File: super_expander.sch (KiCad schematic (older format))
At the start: 48 parts, among them SW1 MCU_RESET, U33 ATtiny85-20SU, U34 PCA9548APW, Y1 8MHz

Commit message: Continue Routing
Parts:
- added C35, C36, C37, C38: 100nF, Capacitor_SMD:C_0603_1608Metric, symbol Device:C_Small
- added C41, C42: 100uF, Capacitor_THT:CP_Radial_D6.3mm_P2.50mm, symbol Device:CP
- added D1: 1N5819, Diode_SMD:D_SOD-123F, symbol Diode:1N5819
- added D2, D3: 0603ESDA-05N, Diode_SMD:D_0603_1608Metric, symbol Device:D_TVS
- added D4: LED_I2C, LED_SMD:LED_0603_1608Metric, symbol Device:LED
- added D5: ZMM6V2, Diode_SMD:D_MiniMELF, symbol Device:D_Zener
- added FB1, FB2: FCM1608KF-121T05, Inductor_SMD:L_0603_1608Metric, symbol Device:Ferrite_Bead_Small
- added J65: USB_B_Micro, Connector_USB:USB_Micro-B_Molex_47346-0001, symbol Connector:USB_B_Micro
- added J66, J67: I2C Passthrough, Connector_PinHeader_2.54mm:PinHeader_1x05_P2.54mm_Vertical, symbol Connector:Conn_01x05_Female
- added J68: Barrel_Jack_Switch, Connector_BarrelJack:BarrelJack_Horizontal, symbol Connector:Barrel_Jack_Switch
- added JP4, JP5, JP6, JP7: I2C BUF PASS, Resistor_SMD:R_0402_1005Metric, symbol Device:Jumper_NO_Small
- added Q1: IRF7410, Package_SO:SOIC-8_3.9x4.9mm_P1.27mm, symbol super_expander:IRF7410
- added R1: 1k, Resistor_SMD:R_0603_1608Metric, symbol Device:R
- added R2: 100k, Resistor_SMD:R_0603_1608Metric, symbol Device:R
- added U35: MCP2221A-I/ST, Package_SO:TSSOP-14_4.4x5mm_P0.65mm, symbol Interface_USB:MCP2221AxST
- added U36, U37: TCA9517, Package_SO:VSSOP-8_3.0x3.0mm_P0.65mm, symbol super_expander:TCA9517
- SW1: footprint Button_Switch_THT:SW_PUSH_6mm -> super_expander:TS-1101
- renumbered C35 to C39, C36 to C40
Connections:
- net +5V: now also C35.1, C36.1, C37.1, C38.1, C41.1, C42.1, D1.1 (K), D5.1 (K), J66.1 (Pin_1), J67.1 (Pin_1), Q1.1 (S), Q1.2 (S), Q1.3 (S), R1.1, U35.1 (VDD), U36.1 (VCCA), U36.5 (EN), U36.8 (VCCB), U37.1 (VCCA), U37.5 (EN), U37.8 (VCCB); no longer C16.1, C19.1, C20.1
- net GND: now also C35.2, C36.2, C37.2, C38.2, C41.2, C42.2, D2.2 (A2), D3.2 (A2), FB2.2, J65.5 (GND), J66.5 (Pin_5), J67.5 (Pin_5), J68.2, J68.3, R2.2, U35.14 (VSS), U36.4 (GND), U37.4 (GND)
- net ~RST: now also J66.4 (Pin_4), J67.4 (Pin_4), U35.7 (GP2)
- net SCL: now reaches U33.7 (PB2), U34.22 (SCL)
- net SCL: now also RN1.3 (R3.1), JP4.2, JP5.1, U35.10 (SCL), U36.7 (SCLB), U37.2 (SCLA); no longer RN1.4 (R4.1)
- net SDA: now reaches U33.5 (AREF/PB0), U34.23 (SDA)
- net SDA: now also RN1.1 (R1.1), JP6.2, JP7.1, U35.9 (SDA), U36.6 (SDAB), U37.3 (SDAA); no longer RN1.3 (R3.1)
- net ~MRST: now reaches SW1.1, U33.1 (~RESET~/PB5)
- net ~MRST: now also RN1.4 (R4.1), U35.4 (~RST); no longer RN1.1 (R1.1)
- new net: C16.1, C19.1, C20.1, U35.11 (VUSB)
- new net: D2.1 (A1), J65.2 (D-), U35.12 (D-)
- new net: D3.1 (A1), J65.3 (D+), U35.13 (D+)
- new net: D4.1 (K), U35.8 (GP3)
- new net: FB1.1, J65.1 (VBUS)
- new net: FB2.1, J65.6 (Shield)
- new net: D1.2 (A), FB1.2
- new net: D4.2 (A), R1.2
- new net: J66.2 (Pin_2), JP4.1, U36.2 (SCLA)
- new net: J66.3 (Pin_3), JP6.1, U36.3 (SDAA)
- new net: J67.3 (Pin_3), JP7.2, U37.6 (SDAB)
- new net: J67.2 (Pin_2), JP5.2, U37.7 (SCLB)
- new net: J68.1, Q1.5 (D), Q1.6 (D), Q1.7 (D), Q1.8 (D)
- new net: D5.2 (A), Q1.4 (G), R2.1
- no-connect marks 0 -> 5
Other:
- moved on the sheet: C15, C16, C17, C18, C19, C20, C21, C22, C23, C24, C25, C26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

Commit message: version 1
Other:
- note added: "Decoupling Caps"
- note added: "I2C Buffer"
- note added: "MCP2221 USB Control"
- note added: "MCU and I2C Mux"
- note added: "Power"
- moved on the sheet: C15, C16, C19, C20, C41, C42, D1, D2, D3, D4, D5, FB1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

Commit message: Add programming header
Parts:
- added J69: ICSP, Connector_PinHeader_2.54mm:PinHeader_2x03_P2.54mm_Vertical, symbol Connector_Generic:Conn_02x03_Odd_Even
- added RN134: 4k7, Resistor_SMD:R_Array_Convex_4x0603, symbol Device:R_Pack04
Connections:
- net +5V: now also J69.2 (Pin_2)
- net GND: now also J69.6 (Pin_6)
- net SCL: now also RN1.4 (R4.1), RN134.7 (R2.2); no longer RN1.3 (R3.1), U33.7 (PB2)
- net SDA: now also RN1.3 (R3.1), RN134.6 (R3.2); no longer RN1.1 (R1.1), U33.5 (AREF/PB0)
- net ~MRST: now also RN1.1 (R1.1), J69.5 (Pin_5); no longer RN1.4 (R4.1)
- net ~RST: now also RN134.8 (R1.2); no longer U33.6 (PB1)
- new net: J69.4 (Pin_4), RN134.3 (R3.1), U33.5 (AREF/PB0)
- new net: J69.1 (Pin_1), RN134.1 (R1.1), U33.6 (PB1)
- new net: J69.3 (Pin_3), RN134.2 (R2.1), U33.7 (PB2)
- no-connect marks 5 -> 7
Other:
- note added: "ATtiny85 MCU"
- note added: "I2C Mux"
- note removed: "MCU and I2C Mux"
- moved on the sheet: C39, C40, JP1, JP2, JP3, RN1, RN2, RN3, RN4, RN5, SW1, U33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

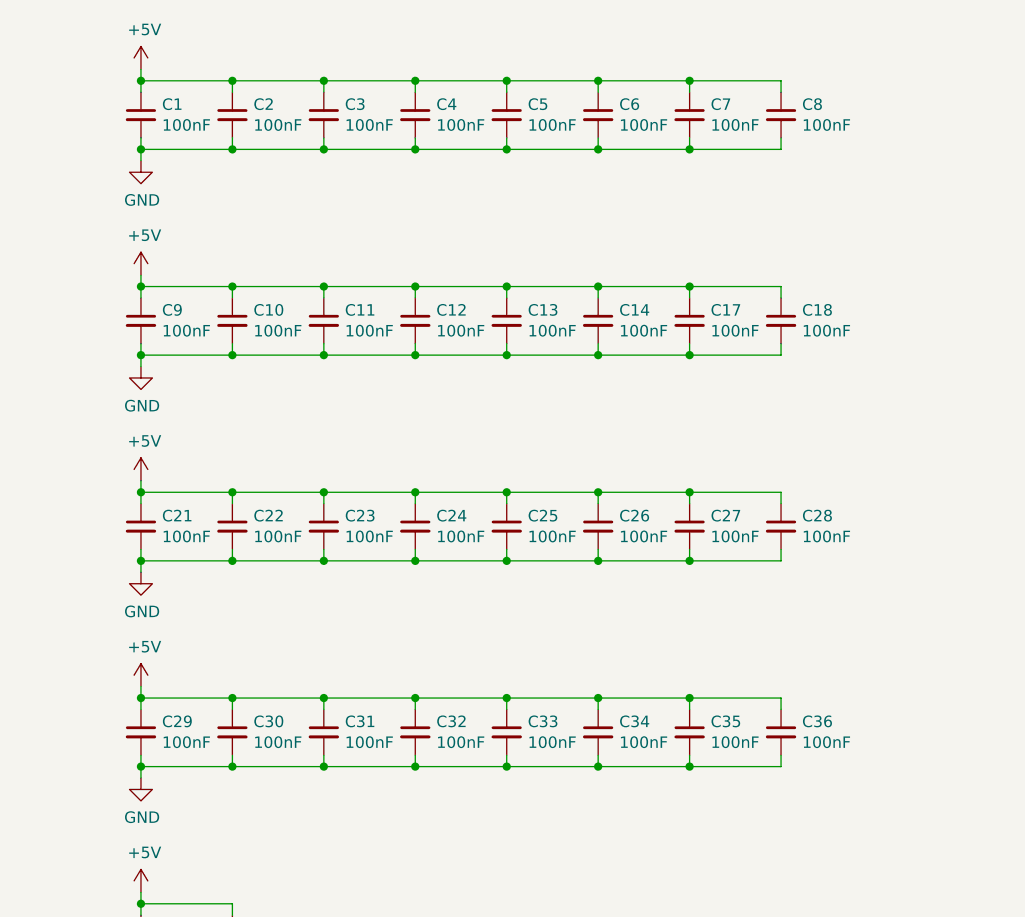
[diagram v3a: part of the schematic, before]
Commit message: Change some C and R values
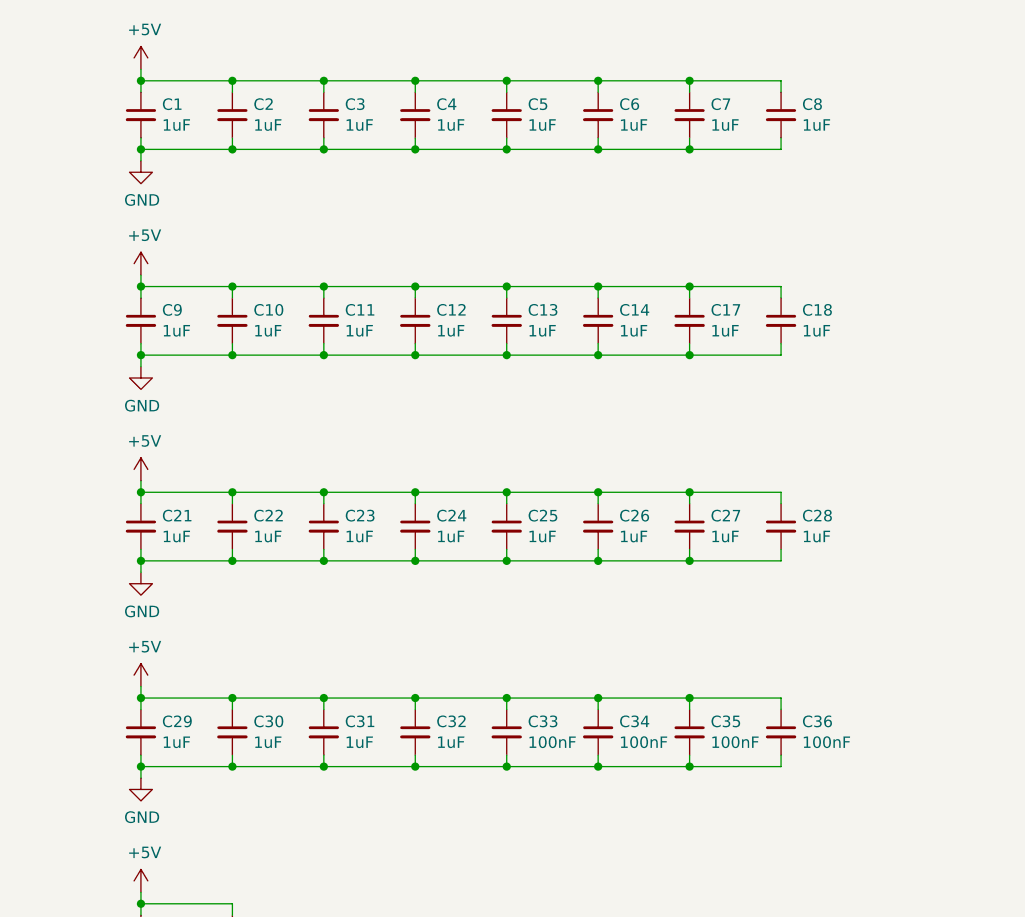
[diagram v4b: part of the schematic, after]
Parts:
- C1, C10, C11, C12, C13, C14, C17, C18, C2, C21, C22, C23, C24, C25, C26, C27, C28, C29, C3, C30, C31, C32, C4, C5, C6, C7, C8, C9: value 100nF -> 1uF
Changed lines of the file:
@@
 P 10100 1550
 F 0 "C1" H 10192 1596 50  0000 L CNN
-F 1 "100nF" H 10192 1505 50  0000 L CNN
+F 1 "1uF" H 10192 1505 50  0000 L CNN
 F 2 "Capacitor_SMD:C_0603_1608Metric" H 10100 1550 50  0001 C CNN
 F 3 "~" H 10100 1550 50  0001 C CNN
@@
 P 10500 1550
 F 0 "C2" H 10592 1596 50  0000 L CNN
-F 1 "100nF" H 10592 1505 50  0000 L CNN
+F 1 "1uF" H 10592 1505 50  0000 L CNN
 F 2 "Capacitor_SMD:C_0603_1608Metric" H 10500 1550 50  0001 C CNN
 F 3 "~" H 10500 1550 50  0001 C CNN
@@
 P 10900 1550
 F 0 "C3" H 10992 1596 50  0000 L CNN
-F 1 "100nF" H 10992 1505 50  0000 L CNN
+F 1 "1uF" H 10992 1505 50  0000 L CNN
 F 2 "Capacitor_SMD:C_0603_1608Metric" H 10900 1550 50  0001 C CNN
 F 3 "~" H 10900 1550 50  0001 C CNN
@@
 P 11300 1550
 F 0 "C4" H 11392 1596 50  0000 L CNN
-F 1 "100nF" H 11392 1505 50  0000 L CNN
+F 1 "1uF" H 11392 1505 50  0000 L CNN
 F 2 "Capacitor_SMD:C_0603_1608Metric" H 11300 1550 50  0001 C CNN
 F 3 "~" H 11300 1550 50  0001 C CNN
@@
 P 11700 1550
 F 0 "C5" H 11792 1596 50  0000 L CNN
-F 1 "100nF" H 11792 1505 50  0000 L CNN
+F 1 "1uF" H 11792 1505 50  0000 L CNN
 F 2 "Capacitor_SMD:C_0603_1608Metric" H 11700 1550 50  0001 C CNN
 F 3 "~" H 11700 1550 50  0001 C CNN
@@
 P 12100 1550
 F 0 "C6" H 12192 1596 50  0000 L CNN
-F 1 "100nF" H 12192 1505 50  0000 L CNN
+F 1 "1uF" H 12192 1505 50  0000 L CNN
 F 2 "Capacitor_SMD:C_0603_1608Metric" H 12100 1550 50  0001 C CNN
 F 3 "~" H 12100 1550 50  0001 C CNN
@@
 P 12500 1550
 F 0 "C7" H 12592 1596 50  0000 L CNN
-F 1 "100nF" H 12592 1505 50  0000 L CNN
+F 1 "1uF" H 12592 1505 50  0000 L CNN
 F 2 "Capacitor_SMD:C_0603_1608Metric" H 12500 1550 50  0001 C CNN
 F 3 "~" H 12500 1550 50  0001 C CNN
@@
 P 12900 1550
 F 0 "C8" H 12992 1596 50  0000 L CNN
-F 1 "100nF" H 12992 1505 50  0000 L CNN
+F 1 "1uF" H 12992 1505 50  0000 L CNN
 F 2 "Capacitor_SMD:C_0603_1608Metric" H 12900 1550 50  0001 C CNN
 F 3 "~" H 12900 1550 50  0001 C CNN
@@
 P 10100 2450
 F 0 "C9" H 10192 2496 50  0000 L CNN
-F 1 "100nF" H 10192 2405 50  0000 L CNN
+F 1 "1uF" H 10192 2405 50  0000 L CNN
 F 2 "Capacitor_SMD:C_0603_1608Metric" H 10100 2450 50  0001 C CNN
 F 3 "~" H 10100 2450 50  0001 C CNN
@@
 P 10500 2450
 F 0 "C10" H 10592 2496 50  0000 L CNN
-F 1 "100nF" H 10592 2405 50  0000 L CNN
+F 1 "1uF" H 10592 2405 50  0000 L CNN
 F 2 "Capacitor_SMD:C_0603_1608Metric" H 10500 2450 50  0001 C CNN
 F 3 "~" H 10500 2450 50  0001 C CNN
@@
 P 10900 2450
 F 0 "C11" H 10992 2496 50  0000 L CNN
-F 1 "100nF" H 10992 2405 50  0000 L CNN
+F 1 "1uF" H 10992 2405 50  0000 L CNN
 F 2 "Capacitor_SMD:C_0603_1608Metric" H 10900 2450 50  0001 C CNN
 F 3 "~" H 10900 2450 50  0001 C CNN
@@
 P 11300 2450
 F 0 "C12" H 11392 2496 50  0000 L CNN
-F 1 "100nF" H 11392 2405 50  0000 L CNN
+F 1 "1uF" H 11392 2405 50  0000 L CNN
 F 2 "Capacitor_SMD:C_0603_1608Metric" H 11300 2450 50  0001 C CNN
 F 3 "~" H 11300 2450 50  0001 C CNN
@@
 P 11700 2450
 F 0 "C13" H 11792 2496 50  0000 L CNN
-F 1 "100nF" H 11792 2405 50  0000 L CNN
+F 1 "1uF" H 11792 2405 50  0000 L CNN
 F 2 "Capacitor_SMD:C_0603_1608Metric" H 11700 2450 50  0001 C CNN
 F 3 "~" H 11700 2450 50  0001 C CNN
@@
 P 12100 2450
 F 0 "C14" H 12192 2496 50  0000 L CNN
-F 1 "100nF" H 12192 2405 50  0000 L CNN
+F 1 "1uF" H 12192 2405 50  0000 L CNN
 F 2 "Capacitor_SMD:C_0603_1608Metric" H 12100 2450 50  0001 C CNN
 F 3 "~" H 12100 2450 50  0001 C CNN
@@
 P 12500 2450
 F 0 "C17" H 12592 2496 50  0000 L CNN
-F 1 "100nF" H 12592 2405 50  0000 L CNN
+F 1 "1uF" H 12592 2405 50  0000 L CNN
 F 2 "Capacitor_SMD:C_0603_1608Metric" H 12500 2450 50  0001 C CNN
 F 3 "~" H 12500 2450 50  0001 C CNN
@@
 P 12900 2450
 F 0 "C18" H 12992 2496 50  0000 L CNN
-F 1 "100nF" H 12992 2405 50  0000 L CNN
+F 1 "1uF" H 12992 2405 50  0000 L CNN
 F 2 "Capacitor_SMD:C_0603_1608Metric" H 12900 2450 50  0001 C CNN
 F 3 "~" H 12900 2450 50  0001 C CNN
@@
 P 10100 3350
 F 0 "C21" H 10192 3396 50  0000 L CNN
-F 1 "100nF" H 10192 3305 50  0000 L CNN
+F 1 "1uF" H 10192 3305 50  0000 L CNN
 F 2 "Capacitor_SMD:C_0603_1608Metric" H 10100 3350 50  0001 C CNN
 F 3 "~" H 10100 3350 50  0001 C CNN
@@
 P 10500 3350
 F 0 "C22" H 10592 3396 50  0000 L CNN
-F 1 "100nF" H 10592 3305 50  0000 L CNN
+F 1 "1uF" H 10592 3305 50  0000 L CNN
 F 2 "Capacitor_SMD:C_0603_1608Metric" H 10500 3350 50  0001 C CNN
 F 3 "~" H 10500 3350 50  0001 C CNN
@@
 P 10900 3350
 F 0 "C23" H 10992 3396 50  0000 L CNN
-F 1 "100nF" H 10992 3305 50  0000 L CNN
+F 1 "1uF" H 10992 3305 50  0000 L CNN
 F 2 "Capacitor_SMD:C_0603_1608Metric" H 10900 3350 50  0001 C CNN
 F 3 "~" H 10900 3350 50  0001 C CNN
@@
 P 11300 3350
 F 0 "C24" H 11392 3396 50  0000 L CNN
-F 1 "100nF" H 11392 3305 50  0000 L CNN
+F 1 "1uF" H 11392 3305 50  0000 L CNN
 F 2 "Capacitor_SMD:C_0603_1608Metric" H 11300 3350 50  0001 C CNN
 F 3 "~" H 11300 3350 50  0001 C CNN
@@
 P 11700 3350
 F 0 "C25" H 11792 3396 50  0000 L CNN
-F 1 "100nF" H 11792 3305 50  0000 L CNN
+F 1 "1uF" H 11792 3305 50  0000 L CNN
 F 2 "Capacitor_SMD:C_0603_1608Metric" H 11700 3350 50  0001 C CNN
 F 3 "~" H 11700 3350 50  0001 C CNN
@@
 P 12100 3350
 F 0 "C26" H 12192 3396 50  0000 L CNN
-F 1 "100nF" H 12192 3305 50  0000 L CNN
+F 1 "1uF" H 12192 3305 50  0000 L CNN
 F 2 "Capacitor_SMD:C_0603_1608Metric" H 12100 3350 50  0001 C CNN
 F 3 "~" H 12100 3350 50  0001 C CNN
@@
 P 12500 3350
 F 0 "C27" H 12592 3396 50  0000 L CNN
-F 1 "100nF" H 12592 3305 50  0000 L CNN
+F 1 "1uF" H 12592 3305 50  0000 L CNN
 F 2 "Capacitor_SMD:C_0603_1608Metric" H 12500 3350 50  0001 C CNN
 F 3 "~" H 12500 3350 50  0001 C CNN
@@
 P 12900 3350
 F 0 "C28" H 12992 3396 50  0000 L CNN
-F 1 "100nF" H 12992 3305 50  0000 L CNN
+F 1 "1uF" H 12992 3305 50  0000 L CNN
 F 2 "Capacitor_SMD:C_0603_1608Metric" H 12900 3350 50  0001 C CNN
 F 3 "~" H 12900 3350 50  0001 C CNN
@@
 P 11300 4250
 F 0 "C32" H 11392 4296 50  0000 L CNN
-F 1 "100nF" H 11392 4205 50  0000 L CNN
+F 1 "1uF" H 11392 4205 50  0000 L CNN
 F 2 "Capacitor_SMD:C_0603_1608Metric" H 11300 4250 50  0001 C CNN
 F 3 "~" H 11300 4250 50  0001 C CNN
@@
 P 10900 4250
 F 0 "C31" H 10992 4296 50  0000 L CNN
-F 1 "100nF" H 10992 4205 50  0000 L CNN
+F 1 "1uF" H 10992 4205 50  0000 L CNN
 F 2 "Capacitor_SMD:C_0603_1608Metric" H 10900 4250 50  0001 C CNN
 F 3 "~" H 10900 4250 50  0001 C CNN
@@
 P 10500 4250
 F 0 "C30" H 10592 4296 50  0000 L CNN
-F 1 "100nF" H 10592 4205 50  0000 L CNN
+F 1 "1uF" H 10592 4205 50  0000 L CNN
 F 2 "Capacitor_SMD:C_0603_1608Metric" H 10500 4250 50  0001 C CNN
 F 3 "~" H 10500 4250 50  0001 C CNN
@@
 P 10100 4250
 F 0 "C29" H 10192 4296 50  0000 L CNN
-F 1 "100nF" H 10192 4205 50  0000 L CNN
+F 1 "1uF" H 10192 4205 50  0000 L CNN
 F 2 "Capacitor_SMD:C_0603_1608Metric" H 10100 4250 50  0001 C CNN
 F 3 "~" H 10100 4250 50  0001 C CNN
